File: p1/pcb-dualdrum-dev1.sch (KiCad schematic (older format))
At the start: 248 parts

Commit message: setup power
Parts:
- removed C? (x3): 10uF, 4ms_Capacitor:CP_Elec_5x5.3, symbol 4ms-passives:CP1_Small
- removed C? (x4): 220pF, 4ms_Capacitor:C_0603, symbol 4ms-passives:C_Small
- removed C? (x4): 1uF, 4ms_Capacitor:C_0603, symbol 4ms-passives:C_Small
- removed C? (x11): 0.1uF, 4ms_Capacitor:C_0603, symbol 4ms-passives:C_Small
- removed C?: 22uF, 4ms_Capacitor:C_0805, symbol 4ms-passives:C_Small
- removed C? (x2): 10uF 16v, 4ms_Capacitor:C_0805, symbol 4ms-passives:C_Small
- removed C? (x2): 47uF, 4ms_Capacitor:CP_Elec_5x5.3, symbol 4ms-passives:CP1_Small
- removed C?: 20pF, 4ms_Capacitor:C_0603, symbol 4ms-passives:C_Small
- removed D?: B140HW-7, 4ms_Diode:D_SOD-123, symbol 4ms-passives:D_Schottky
- removed D? (x5): SD103, 4ms_Diode:D_SOD-323F, symbol 4ms-passives:D
- removed D? (x2): B140HW-7, 4ms_Diode:D_SOD-123, symbol 4ms-passives:B140HW-7
- removed ENV_LED?, GATE_LED?, INV_LED?: LED, 4ms_LED:LED_0603_1608Metric, symbol 4ms-passives:LED
- removed EnvSense?, Level_?: 100k, 4ms_Potentiometer:Pot_9mm_Knurl_NoDet, symbol 4ms-mech:POT
- removed GATE? (x2), INL? (x2): JACK-MONO, 4ms_Jack:EighthInch_PJ398SM, symbol 4ms-mech:JACK-MONO
- removed J?: Conn_02x04_Odd_Even, 4ms_Connector:Pins_2x04_2.54mm_TH, symbol 4ms-headers:Conn_02x04_Odd_Even
- removed LED?: RGB, 4ms_LED:LED_PLCC-4, symbol 4ms-passives:LED-RGB-CA
- removed Level_? (x2): 100k, 4ms_Potentiometer:Pot_16mm_NoDet_RV16AF-4A, symbol 4ms-mech:POT
- removed P?: CONN-02x05, 4ms_Connector:Pins_2x05_2.54mm_TH_Europower, symbol 4ms-headers:EURO_HEADER_10pin
- removed Q? (x2): MBT3904DW1, 4ms_Package_SOT:SOT-363_SC-70-6, symbol 4ms-ic:MBT3904DW1
- removed R? (x4): 20k, 4ms_Resistor:R_0603, symbol 4ms-passives:R
- removed R? (x16): 1k, 4ms_Resistor:R_0603, symbol 4ms-passives:R
- removed R? (x6): 10k, 4ms_Resistor:R_0603, symbol 4ms-passives:R
- removed R? (x2): 100K, 4ms_Resistor:R_0603, symbol 4ms-passives:R
- removed R? (x7): 100k, 4ms_Resistor:R_0603, symbol 4ms-passives:R
- removed R?: 330, 4ms_Resistor:R_0603, symbol 4ms-passives:R
- removed R? (x2): 47k, 4ms_Resistor:R_0603, symbol 4ms-passives:R
- removed R?: 22k, 4ms_Resistor:R_0603, symbol 4ms-passives:R
- removed R?: 33k, 4ms_Resistor:R_0603, symbol 4ms-passives:R
- removed R?: 10K, 4ms_Resistor:R_0603, symbol 4ms-passives:R
- removed R?: 4K7, 4ms_Resistor:R_0603, symbol 4ms-passives:R
- removed R?: 49k9, 4ms_Resistor:R_0603, symbol 4ms-passives:R
- removed R?: 4k7, 4ms_Resistor:R_0603, symbol 4ms-passives:R
- removed R?: 13k, 4ms_Resistor:R_0603, symbol 4ms-passives:R
- removed R?: 1M, 4ms_Resistor:R_0603, symbol 4ms-passives:R
- removed R?: 2k, 4ms_Resistor:R_0603, symbol 4ms-passives:R
- removed R?: 100k - used to be 1k, 4ms_Resistor:R_0603, symbol 4ms-passives:R
- removed R? (x2): 220, 4ms_Resistor:R_0603, symbol 4ms-passives:R
- removed SW?: SPST, 4ms_Switch:Slide_Switch_Runrun_SS22D06, symbol 4ms-mech:DPDT-shielded-sep
- removed SW? (x2): SW_SPDT, symbol 4ms-mech:SW_SPDT
- removed TR?: 100k, 4ms_Potentiometer:Pot_Trim_SMT_TC33X, symbol 4ms-mech:TRIMPOT
- removed U?: LMC7660, symbol Regulator_SwitchedCapacitor:LMC7660
- removed U? (x2): LM13700, symbol Amplifier_Operational:LM13700
- removed U? (x13): 082, 4ms_Package_SSOP:TSSOP-8_4.4x3mm_Pitch0.65mm, symbol 4ms-ic:NJM2068-separate-power
- removed U? (x4): NJM, 4ms_Package_SSOP:TSSOP-8_4.4x3mm_Pitch0.65mm, symbol 4ms-ic:NJM2068-separate-power
- removed U? (x5): CD4001, 4ms_Package_SOIC:SOIC-14_3.9x8.65mm_Pitch1.27mm, symbol 4ms-ic:4001
- added C? (x2): 220pF, 4ms_Capacitor:C_0603, symbol 4ms-passives:C_Small
- added C?: 1uF, 4ms_Capacitor:C_0603, symbol 4ms-passives:C_Small
- added C? (x28): 0.1uF, 4ms_Capacitor:C_0603, symbol 4ms-passives:C_Small
- added C? (x2): 47uF, 4ms_Capacitor:CP_Elec_5x5.3, symbol 4ms-passives:CP1_Small
- added D? (x2): B140HW-7, 4ms_Diode:D_SOD-123, symbol 4ms-passives:B140HW-7
- added Level_?: 100k, 4ms_Potentiometer:Pot_16mm_NoDet_RV16AF-4A, symbol 4ms-mech:POT
- added MIC/LINE1, MIC/LINE2: SPST, 4ms_Switch:Slide_Switch_Runrun_SS22D06, symbol 4ms-mech:DPDT-shielded-sep
- added P?: CONN-02x05, 4ms_Connector:Pins_2x05_2.54mm_TH_Europower, symbol 4ms-headers:EURO_HEADER_10pin
- added R?: 10k, 4ms_Resistor:R_0603, symbol 4ms-passives:R
- added R?: 100k, 4ms_Resistor:R_0603, symbol 4ms-passives:R
- added R?: 100K, 4ms_Resistor:R_0603, symbol 4ms-passives:R
- added R? (x4): 1k, 4ms_Resistor:R_0603, symbol 4ms-passives:R
- added R?: 220, 4ms_Resistor:R_0603, symbol 4ms-passives:R
- added R? (x3): 20k, 4ms_Resistor:R_0603, symbol 4ms-passives:R
- added U? (x9): 082, 4ms_Package_SSOP:TSSOP-8_4.4x3mm_Pitch0.65mm, symbol 4ms-ic:NJM2068-separate-power
- added U? (x3): NJM, 4ms_Package_SSOP:TSSOP-8_4.4x3mm_Pitch0.65mm, symbol 4ms-ic:NJM2068-separate-power
- added U? (x2): CD4001, 4ms_Package_SOIC:SOIC-14_3.9x8.65mm_Pitch1.27mm, symbol 4ms-ic:4001
- added U? (x3): LM13700, symbol Amplifier_Operational:LM13700
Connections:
- net labels removed: -9V, In_LED, audio_thru, env_out, exp_jack_input, exp_sw_in, exp_sw_out, inv_out
- wire segments 460 -> 321
- no-connect marks 29 -> 22
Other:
- note removed: "-results in -20mV"
- note removed: "ENVELOPES"
- note removed: "EXPANDER \nHEADER"
- note removed: "For triggering with sts\nR3 = 220\nR5 = 10k\n\nfor mics\nR3 = 100K-113k\nR5 = 10k"
- note removed: "INPUT"
- note removed: "INPUT CLIP"
- note removed: "ONE-SHOT/GATE"
- note removed: "\n"
- note removed: "necesita proteccio de polaridad?"
- note removed: "need to put jumper for parallel resistor\nif R5 stays at 10k, need to make R3 100k in mic trigger mode, but 220 in sts mode\n"
- note removed: "use the new 8 pin header and add a jumper switch on the expansion module!"
- moved on the sheet: R?, U?B, U?D, U?E

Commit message: about to annotate parts
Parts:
- added AUDIO_OUT1, AUDIO_OUT2: JACK-MONO, 4ms_Jack:EighthInch_PJ398SM, symbol 4ms-mech:JACK-MONO
- added Bypass_2nd_Filter1, Bypass_2nd_Filter?: Conn_01x03, symbol 4ms-headers:Conn_01x03
- added R? (x2): 1k, 4ms_Resistor:R_0603, symbol 4ms-passives:R
- gave numbers to parts that had none: 2
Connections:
- net GND: now also AUDIO_OUT1.2 (SHEILD), AUDIO_OUT2.2 (SHEILD)
- net at R?.1, R?.1, U?.1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: now also Bypass_2nd_Filter1.2 (Pin_2); no longer R?.1
- net at C?.2, R?.1, R?.2: now also R?.1 (x2)
- net at R?.1, R?.1, U?.1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: now also Bypass_2nd_Filter?.2 (Pin_2); no longer R?.1
- net at R?.1, R?.1, U?.1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: now also Bypass_2nd_Filter?.1 (Pin_1)
- net at R?.1, R?.1, U?.1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: now also Bypass_2nd_Filter1.1 (Pin_1)
- new net: AUDIO_OUT1.1 (SIG), R?.2
- new net: AUDIO_OUT2.1 (SIG), R?.2
- new net: Bypass_2nd_Filter1.3 (Pin_3), R?.1
- new net: Bypass_2nd_Filter?.3 (Pin_3), R?.1
- no-connect marks 22 -> 24
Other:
- note added: "try to jumper some of the unity gain followers"
- moved on the sheet: C?, D?, GATE_LED?, GATE_OUT1, GATE_OUT2, Level_?, MIC/LINE2A, R?, TR?, U?A, U?B, U?C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

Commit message: grouped components
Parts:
- added unit 2 of LM1
- added unit 4 of LM1
- added unit 2 of LM2
- added unit 4 of LM2
- Bypass_2nd_Filter1: footprint (none) -> 4ms_Connector:Pins_1x03_2.54mm_TH
- Bypass_2nd_Filter2: renamed from Bypass_2nd_Filter?; footprint (none) -> 4ms_Connector:Pins_1x03_2.54mm_TH
- LM1, LM2, LM3, LM4: renamed from U?; footprint (none) -> 4ms_Package_SOIC:SOIC-16_3.9x9.9mm_Pitch1.27mm
- MIC/LINE1, MIC/LINE2: footprint 4ms_Switch:Slide_Switch_Runrun_SS22D06 -> 4ms_Switch:Switch_Toggle_SPDT_SubMini
- U1, U2, U3, U4, U7: renamed from U?; value NJM -> 082
- U5: renamed from U?; value 072 -> 082
- U8: renamed from U?; value NJM -> 082-NJM
- U8: renamed from U?; value 082 -> 082-NJM
- gave numbers to parts that had none: 137
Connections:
- net +9V is gone; now on net +12V: R1.1, R32.1
- net GND: now also U6.5 (+), U7.5 (+), U8.3 (+); no longer U6.3 (+), U7.3 (+), U8.5 (+)
- net at C5.1, LM1.5: now also U1.5 (+); no longer U1.3 (+)
- net at R16.2, R9.1: now also U9.3 (+); no longer U9.5 (+)
- net at R14.2, R18.1: now also U9.1, U9.2 (-); no longer U9.6 (-), U9.7
- net at Bypass_2nd_Filter1.1 (Pin_1), R26.1, R30.1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: now also U6.3 (+); no longer U6.5 (+)
- net at Bypass_2nd_Filter2.1 (Pin_1), R56.1, R61.1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: now also U7.3 (+); no longer U7.5 (+)
- net at IN2.3 (SW), R4.1: now also U5.1, U5.2 (-); no longer U5.6 (-), U5.7
- net at C15.1, LM3.5: now also U3.5 (+); no longer U3.3 (+)
- net at C20.1, LM4.5: now also U4.5 (+); no longer U4.3 (+)
- net at C16.2, R39.2, R43.2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: now also U7.7; no longer U7.1
- net at R48.1: now also U7.6 (-); no longer U7.2 (-)
- net at C1.2, R5.2: now also U5.3 (+); no longer U5.5 (+)
- net at C10.1, LM2.5: now also U2.5 (+); no longer U2.3 (+)
- net at C6.2, R15.2, R20.2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: now also U6.7; no longer U6.1
- net at R19.1: now also U6.6 (-); no longer U6.2 (-)
- net at C3.2, C8.1, Level_1.1 (Left): now also U8.1; no longer U8.7
- net at C3.1, Level_1.2 (Center), R20.1: now also U8.2 (-); no longer U8.6 (-)
- new net: R21.1, U1.6 (-), U1.7
- new net: R50.1, U3.6 (-), U3.7
- new net: R62.1, U4.6 (-), U4.7
- new net: R48.2, U7.1, U7.2 (-)
- new net: R31.1, U2.6 (-), U2.7
- new net: R19.2, U6.1, U6.2 (-)
- no-connect marks 24 -> 32
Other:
- moved on the sheet: C32, C33, C34, C35, C36, C37, C38, C39, C40, C41, C43, C44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

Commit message: cruisin
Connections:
- net +12V: now also C29.1
- net -12VA: now also C31.2
- net at C4.1, LM1.12: now also U1.5 (+); no longer U1.3 (+)
- net at C5.1, LM1.5: now also U1.3 (+); no longer U1.5 (+)
- net at Bypass_2nd_Filter1.2 (Pin_2), R17.1, R7.1: now also U1.6 (-), U1.7; no longer U1.1, U1.2 (-)
- net at Bypass_2nd_Filter1.1 (Pin_1), R26.1, R30.1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: now also U2.6 (-), U2.7; no longer U2.1, U2.2 (-)
- net at Bypass_2nd_Filter2.1 (Pin_1), R56.1, R61.1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: now also U4.6 (-), U4.7; no longer U4.1, U4.2 (-)
- net at Bypass_2nd_Filter2.2 (Pin_2), R38.1, R44.1: now also U3.6 (-), U3.7; no longer U3.1, U3.2 (-)
- net at C14.1, LM3.12: now also U3.5 (+); no longer U3.3 (+)
- net at C15.1, LM3.5: now also U3.3 (+); no longer U3.5 (+)
- net at C19.1, LM4.12: now also U4.5 (+); no longer U4.3 (+)
- net at C20.1, LM4.5: now also U4.3 (+); no longer U4.5 (+)
- net at R48.1, U7.6 (-): now also C16.1, MIC/LINE2.2 (B)
- net at C9.1, LM2.12: now also U2.5 (+); no longer U2.3 (+)
- net at C10.1, LM2.5: now also U2.3 (+); no longer U2.5 (+)
- net at R19.1, U6.6 (-): now also C6.1, MIC/LINE1.2 (B)
- new net: R21.1, U1.1, U1.2 (-)
- new net: R50.1, U3.1, U3.2 (-)
- new net: R62.1, U4.1, U4.2 (-)
- new net: R31.1, U2.1, U2.2 (-)
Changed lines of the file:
@@
 $Comp
 L 4ms-ic:NJM2068-separate-power U?
-U 1 1 5D96046E
+U 2 1 5D96046E
 P 4975 1825
 AR Path="/5B8C674E/5D96046E" Ref="U?"  Part="2"
-AR Path="/5D96046E" Ref="U1"  Part="1"
+AR Path="/5D96046E" Ref="U1"  Part="2"
 AR Path="/5D4A5981/5D96046E" Ref="U?"  Part="1"
 F 0 "U1" H 5025 1925 50  0000 L CNN
@@
 F 4 "Mouser" H 1225 -2600 50  0001 C CNN "Manufacturer"
 F 5 "Substitution OK" H 1225 -2600 50  0001 C CNN "Comments"
-	1    4975 1825
+	2    4975 1825
 	1    0    0    -1
 $EndComp
@@
 $Comp
 L 4ms-ic:NJM2068-separate-power U?
-U 2 1 5DD0F3DF
+U 1 1 5DD0F3DF
 P 7100 1850
 AR Path="/5B8C674E/5DD0F3DF" Ref="U?"  Part="2"
-AR Path="/5DD0F3DF" Ref="U1"  Part="2"
+AR Path="/5DD0F3DF" Ref="U1"  Part="1"
 AR Path="/5D4A5981/5DD0F3DF" Ref="U?"  Part="1"
 F 0 "U1" H 7150 1950 50  0000 L CNN
@@
 F 4 "Mouser" H 3350 -2575 50  0001 C CNN "Manufacturer"
 F 5 "Substitution OK" H 3350 -2575 50  0001 C CNN "Comments"
-	2    7100 1850
+	1    7100 1850
 	1    0    0    -1
 $EndComp
@@
 $Comp
 L 4ms-ic:NJM2068-separate-power U?
-U 1 1 5DFB9E5B
+U 2 1 5DFB9E5B
 P 4875 3425
 AR Path="/5B8C674E/5DFB9E5B" Ref="U?"  Part="2"
-AR Path="/5DFB9E5B" Ref="U2"  Part="1"
+AR Path="/5DFB9E5B" Ref="U2"  Part="2"
 AR Path="/5D4A5981/5DFB9E5B" Ref="U?"  Part="1"
 F 0 "U2" H 4925 3525 50  0000 L CNN
@@
 F 4 "Mouser" H 1125 -1000 50  0001 C CNN "Manufacturer"
 F 5 "Substitution OK" H 1125 -1000 50  0001 C CNN "Comments"
-	1    4875 3425
+	2    4875 3425
 	1    0    0    -1
 $EndComp
@@
 $Comp
 L 4ms-ic:NJM2068-separate-power U?
-U 2 1 5DFB9E7E
+U 1 1 5DFB9E7E
 P 7000 3450
 AR Path="/5B8C674E/5DFB9E7E" Ref="U?"  Part="2"
-AR Path="/5DFB9E7E" Ref="U2"  Part="2"
+AR Path="/5DFB9E7E" Ref="U2"  Part="1"
 AR Path="/5D4A5981/5DFB9E7E" Ref="U?"  Part="1"
 F 0 "U2" H 7050 3550 50  0000 L CNN
@@
 F 4 "Mouser" H 3250 -975 50  0001 C CNN "Manufacturer"
 F 5 "Substitution OK" H 3250 -975 50  0001 C CNN "Comments"
-	2    7000 3450
+	1    7000 3450
 	1    0    0    -1
 $EndComp
@@
 $Comp
 L 4ms-ic:NJM2068-separate-power U?
-U 1 1 5DA605CD
+U 2 1 5DA605CD
 P 4925 5850
 AR Path="/5B8C674E/5DA605CD" Ref="U?"  Part="2"
-AR Path="/5DA605CD" Ref="U3"  Part="1"
+AR Path="/5DA605CD" Ref="U3"  Part="2"
 AR Path="/5D4A5981/5DA605CD" Ref="U?"  Part="1"
 F 0 "U3" H 4975 5950 50  0000 L CNN
@@
 F 4 "Mouser" H 1175 1425 50  0001 C CNN "Manufacturer"
 F 5 "Substitution OK" H 1175 1425 50  0001 C CNN "Comments"
-	1    4925 5850
+	2    4925 5850
 	1    0    0    -1
 $EndComp
@@
 $Comp
 L 4ms-ic:NJM2068-separate-power U?
-U 2 1 5DA605F0
+U 1 1 5DA605F0
 P 7050 5875
 AR Path="/5B8C674E/5DA605F0" Ref="U?"  Part="2"
-AR Path="/5DA605F0" Ref="U3"  Part="2"
+AR Path="/5DA605F0" Ref="U3"  Part="1"
 AR Path="/5D4A5981/5DA605F0" Ref="U?"  Part="1"
 F 0 "U3" H 7100 5975 50  0000 L CNN
@@
 F 4 "Mouser" H 3300 1450 50  0001 C CNN "Manufacturer"
 F 5 "Substitution OK" H 3300 1450 50  0001 C CNN "Comments"
-	2    7050 5875
+	1    7050 5875
 	1    0    0    -1
 $EndComp
@@
 $Comp
 L 4ms-ic:NJM2068-separate-power U?
-U 1 1 5DA606CE
+U 2 1 5DA606CE
 P 4825 7450
 AR Path="/5B8C674E/5DA606CE" Ref="U?"  Part="2"
-AR Path="/5DA606CE" Ref="U4"  Part="1"
+AR Path="/5DA606CE" Ref="U4"  Part="2"
 AR Path="/5D4A5981/5DA606CE" Ref="U?"  Part="1"
 F 0 "U4" H 4875 7550 50  0000 L CNN
@@
 F 4 "Mouser" H 1075 3025 50  0001 C CNN "Manufacturer"
 F 5 "Substitution OK" H 1075 3025 50  0001 C CNN "Comments"
-	1    4825 7450
+	2    4825 7450
 	1    0    0    -1
 $EndComp
@@
 $Comp
 L 4ms-ic:NJM2068-separate-power U?
-U 2 1 5DA606F1
+U 1 1 5DA606F1
 P 6950 7475
 AR Path="/5B8C674E/5DA606F1" Ref="U?"  Part="2"
-AR Path="/5DA606F1" Ref="U4"  Part="2"
+AR Path="/5DA606F1" Ref="U4"  Part="1"
 AR Path="/5D4A5981/5DA606F1" Ref="U?"  Part="1"
 F 0 "U4" H 7000 7575 50  0000 L CNN
@@
 F 4 "Mouser" H 3200 3050 50  0001 C CNN "Manufacturer"
 F 5 "Substitution OK" H 3200 3050 50  0001 C CNN "Comments"
-	2    6950 7475
+	1    6950 7475
 	1    0    0    -1
 $EndComp
@@
 	7550 6550 7650 6550
 Wire Wire Line
-	8575 6450 8975 6450
+	8575 6450 8800 6450
 Wire Wire Line
 	8800 6250 8800 6000
@@
 	7600 2525 7700 2525
 Wire Wire Line
-	8625 2425 9025 2425
+	8625 2425 8850 2425
 Wire Wire Line
 	8850 2225 8850 1975
@@
 	0    -1   -1   0
 $EndComp
-$Comp
-L 4ms-passives:CP1_Small C?
-U 1 1 5E8D2826
-P 19600 14175
-AR Path="/5BB43456/5E8D2826" Ref="C?"  Part="1"
-AR Path="/5E8D2826" Ref="C31"  Part="1"
-AR Path="/5E7668A3/5E8D2826" Ref="C?"  Part="1"
-F 0 "C31" H 19675 14150 50  0000 L CNN
-F 1 "47uF" H 19650 14225 50  0000 L CNN
-F 2 "4ms_Capacitor:CP_Elec_5x5.3" H 19600 14175 50  0001 C CNN
-F 3 "" H 19600 14175 50  0000 C CNN
-F 4 "Mouser" H 16925 6775 50  0001 C CNN "Manufacturer"
-F 5 "Substitution OK" H 16925 6775 50  0001 C CNN "Comments"
-F 6 "TEST" H 16925 6775 50  0001 C CNN "Part Number"
-F 7 "2" H 16925 6775 50  0001 C CNN "Points"
-F 8 "SMD" H 16925 6775 50  0001 C CNN "SMD/TH"
-	1    19600 14175
-	-1   0    0    1
-$EndComp
-Wire Wire Line
-	19275 13350 19875 13350
 Wire Wire Line
-	19275 14075 19900 14075
+	19275 13350 19600 13350
 $Comp
 L 4ms-power:+12V #PWR?
@@
 	1    0    0    -1
 $EndComp
+Connection ~ 19600 13350
+Wire Wire Line
+	19600 13350 19875 13350
+$Comp
+L 4ms-passives:CP1_Small C?
+U 1 1 5E8D2826
+P 19600 14175
+AR Path="/5BB43456/5E8D2826" Ref="C?"  Part="1"
+AR Path="/5E8D2826" Ref="C31"  Part="1"
+AR Path="/5E7668A3/5E8D2826" Ref="C?"  Part="1"
+F 0 "C31" H 19675 14150 50  0000 L CNN
+F 1 "47uF" H 19650 14225 50  0000 L CNN
+F 2 "4ms_Capacitor:CP_Elec_5x5.3" H 19600 14175 50  0001 C CNN
+F 3 "" H 19600 14175 50  0000 C CNN
+F 4 "Mouser" H 16925 6775 50  0001 C CNN "Manufacturer"
+F 5 "Substitution OK" H 16925 6775 50  0001 C CNN "Comments"
+F 6 "TEST" H 16925 6775 50  0001 C CNN "Part Number"
+F 7 "2" H 16925 6775 50  0001 C CNN "Points"
+F 8 "SMD" H 16925 6775 50  0001 C CNN "SMD/TH"
+	1    19600 14175
+	-1   0    0    1
+$EndComp
+Wire Wire Line
+	19275 14075 19600 14075
+Wire Wire Line
+	19600 14075 19900 14075
+Connection ~ 19600 14075
+Wire Wire Line
+	8850 2225 8850 2425
+Connection ~ 8850 2225
+Connection ~ 8850 2425
+Wire Wire Line
+	8850 2425 9025 2425
+Wire Wire Line
+	8800 6250 8800 6450
+Connection ~ 8800 6250
+Connection ~ 8800 6450
+Wire Wire Line
+	8800 6450 8975 6450
 $EndSCHEMATC

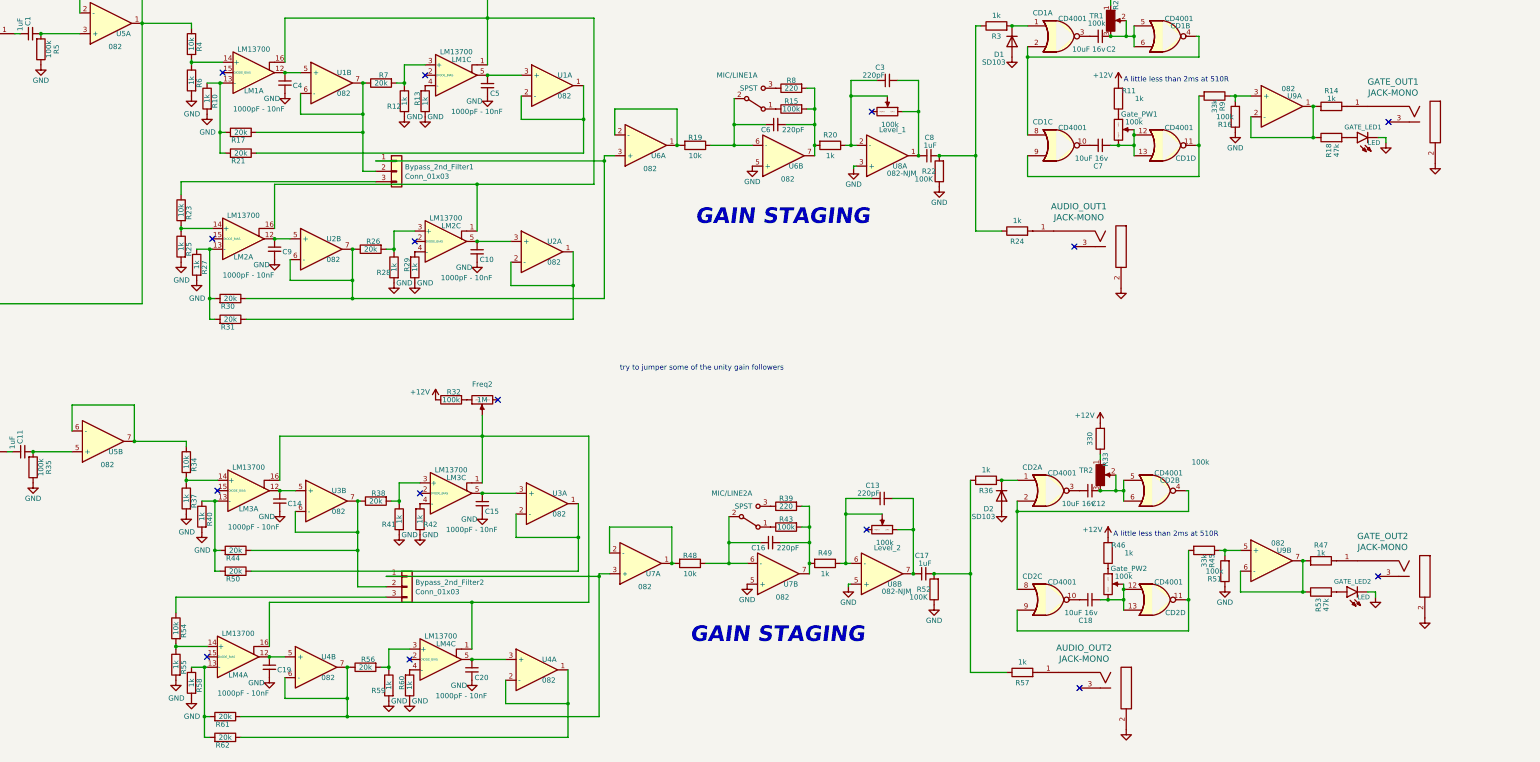
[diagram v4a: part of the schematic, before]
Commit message: beginning to lay tracks
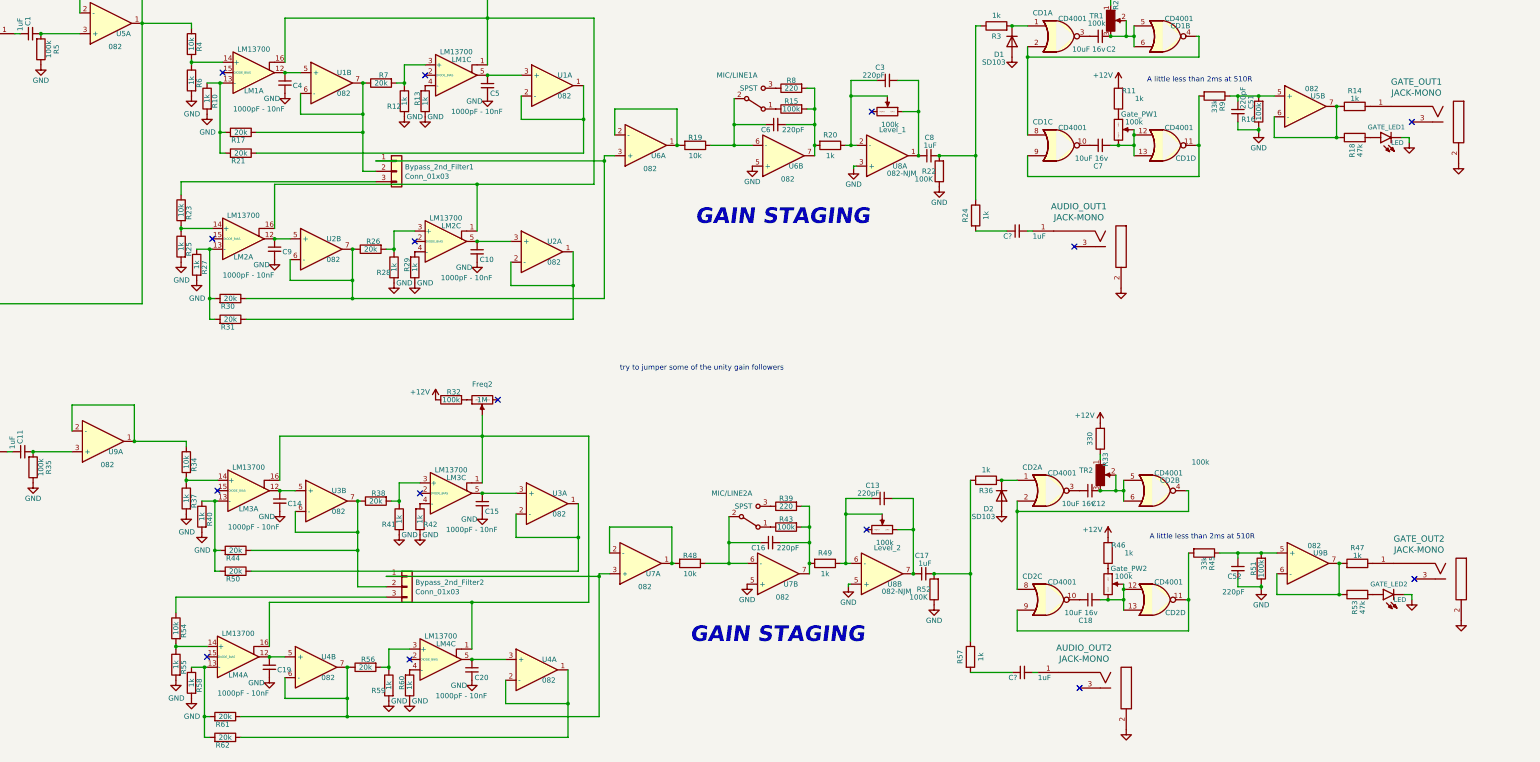
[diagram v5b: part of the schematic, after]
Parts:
- added C51, C52: 220pF, 4ms_Capacitor:C_0603, symbol 4ms-passives:C_Small
- added C? (x2): 1uF, 4ms_Capacitor:C_0603, symbol 4ms-passives:C_Small
- renumbered U9 to U5, U5 to U9
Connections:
- net GND: now also C51.2, C52.2
- net at R14.2, R18.1: now also U5.6 (-), U5.7; no longer U5.1, U5.2 (-)
- net at R16.2, R9.1: now also U5.5 (+), C51.1; no longer U5.3 (+)
- net at R24.2: now also C?.1; no longer AUDIO_OUT1.1 (SIG)
- net at R57.2: now also C?.1; no longer AUDIO_OUT2.1 (SIG)
- net at C11.2, R35.2: now also U9.3 (+); no longer U9.5 (+)
- net at R45.1, R51.2, U9.5 (+): now also C52.1
- new net: AUDIO_OUT1.1 (SIG), C?.2
- new net: AUDIO_OUT2.1 (SIG), C?.2
- new net: R34.1, U9.1, U9.2 (-)
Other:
- moved on the sheet: GATE_LED1, GATE_LED2, GATE_OUT1, GATE_OUT2, R14, R16, R18, R24, R45, R47, R51, R53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
